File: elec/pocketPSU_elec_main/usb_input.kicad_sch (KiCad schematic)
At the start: 15 parts, among them J2 Conn_01x03_Pin, U4 FUSB302MPX

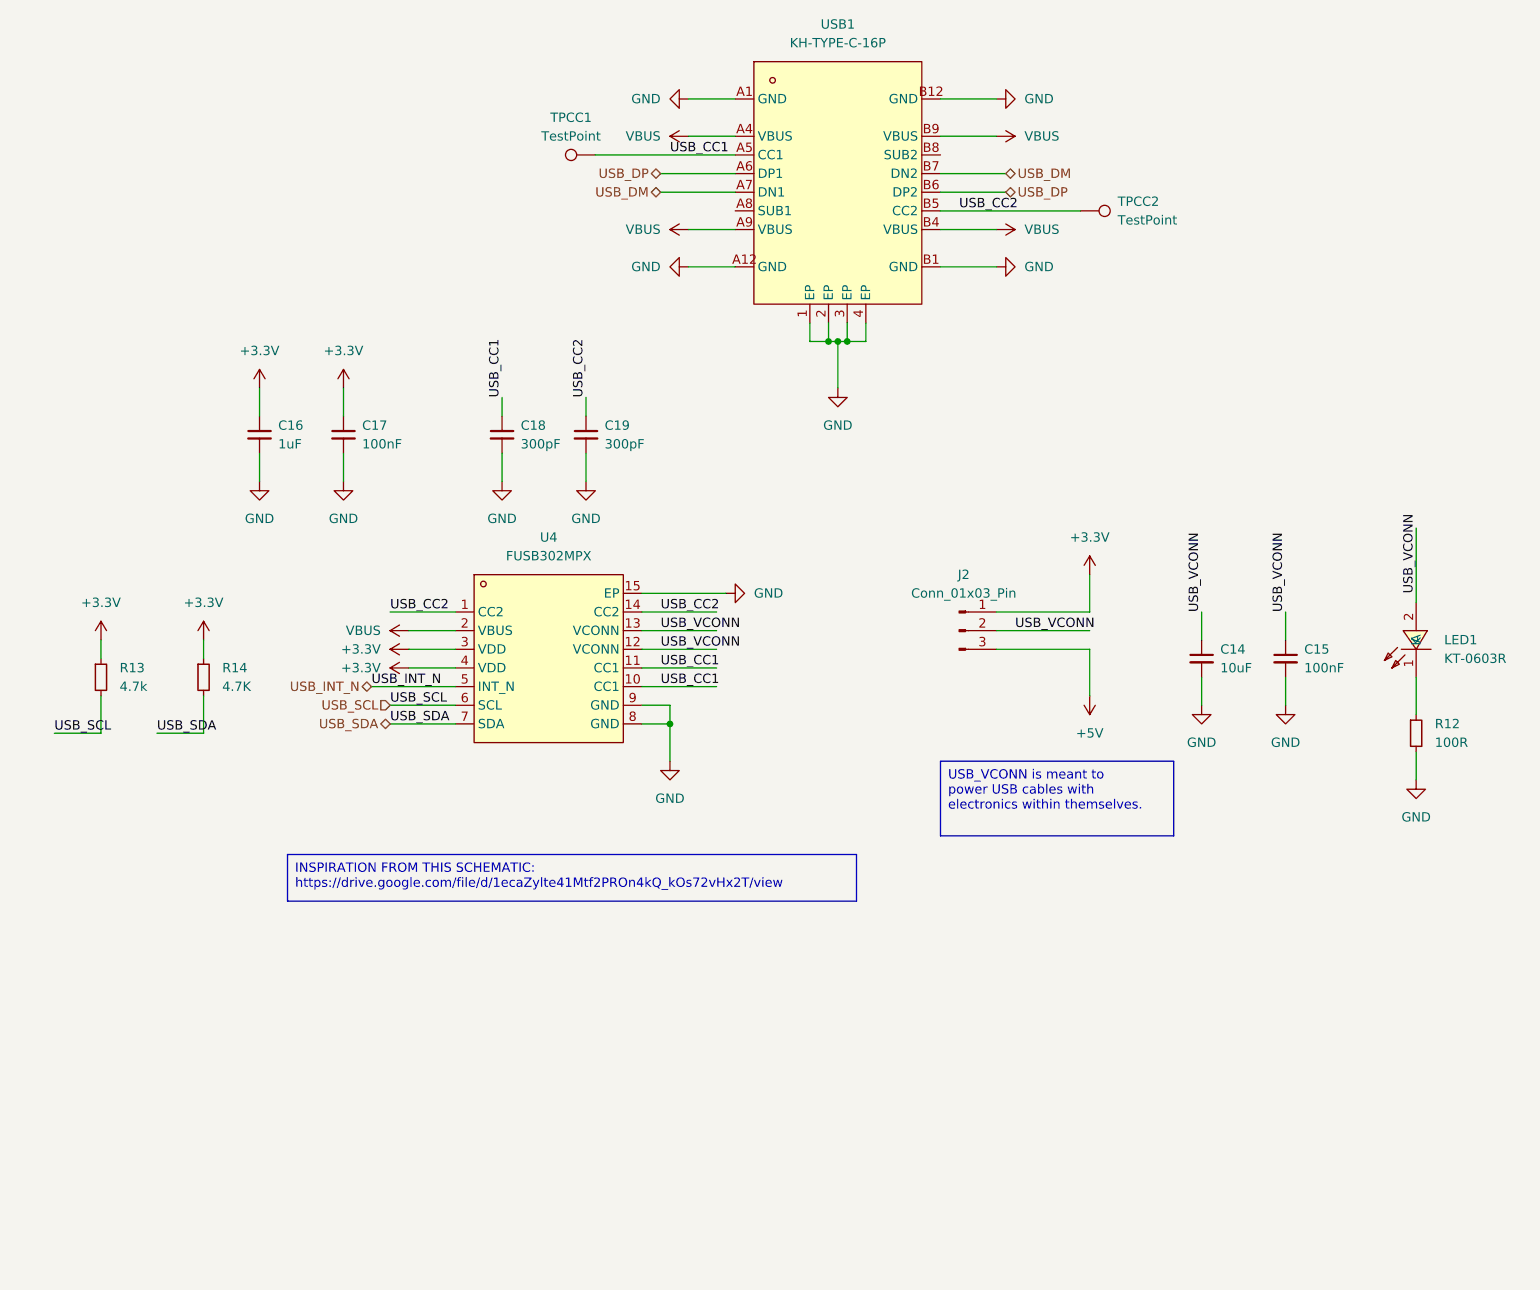
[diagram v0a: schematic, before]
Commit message: Cleanup, Buck, CAN (#6)
* mid-layout

* finished routing

* Kibot (#7)

Add kibot with JLC output generation

* fix 3d, add drc

* fix erc

* fix pcb drc

* drc ignore_unconnected

* attempt to add githash and tag

* add silk githash string

* add silk tag string

* change outputs

---------

Co-authored-by: Jarrod Tuma <jtuma@Jarrods-Laptop.local>
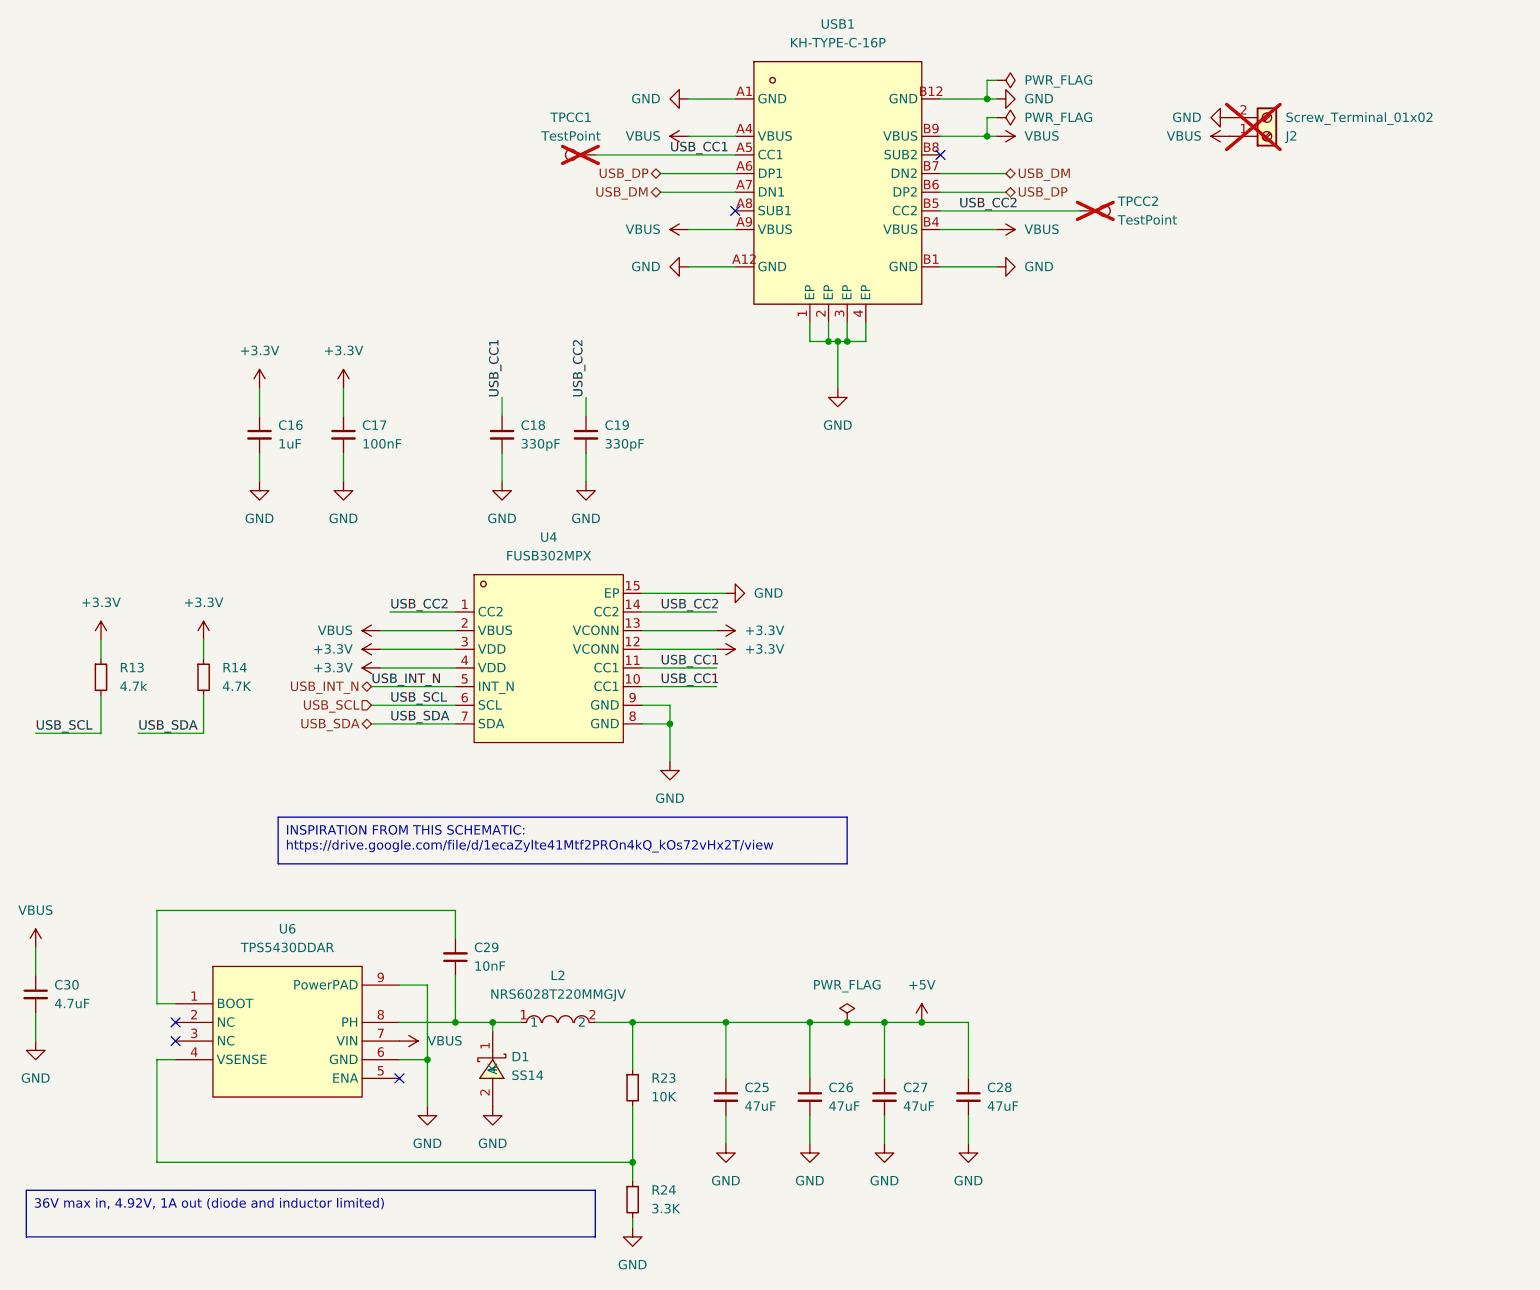
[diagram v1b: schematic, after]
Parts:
- removed C14: 10uF, Capacitor_SMD:C_0805_2012Metric, symbol Device:C_Small
- removed C15: 100nF, Capacitor_SMD:C_0805_2012Metric, symbol Device:C_Small
- removed J2: Conn_01x03_Pin, Connector_PinHeader_1.27mm:PinHeader_1x03_P1.27mm_Vertical, symbol Connector:Conn_01x03_Pin
- removed LED1: KT-0603R, footprints:LED0603-RD, symbol footprints:KT-0603R
- removed R12: 100R, Resistor_SMD:R_0402_1005Metric, symbol Device:R_Small
- added C25, C26, C27, C28: 47uF, Capacitor_SMD:C_1206_3216Metric, symbol Device:C_Small
- added C29: 10nF, Capacitor_SMD:C_0402_1005Metric, symbol Device:C_Small
- added C30: 4.7uF, Capacitor_SMD:C_1206_3216Metric, symbol Device:C_Small
- added D1: SS14, footprints:SMA_L4.2-W2.6-LS5.3-RD, symbol footprints:SS14
- added J2: Screw_Terminal_01x02, TerminalBlock_Phoenix:TerminalBlock_Phoenix_MPT-0,5-2-2.54_1x02_P2.54mm_Horizontal, symbol Connector:Screw_Terminal_01x02
- added L2: NRS6028T220MMGJV, footprints:IND-SMD_L6.0-W6.0, symbol footprints:NRS6028T220MMGJV
- added R23: 10K, Resistor_SMD:R_0402_1005Metric, symbol Device:R_Small
- added R24: 3.3K, Resistor_SMD:R_0402_1005Metric, symbol Device:R_Small
- added U6: TPS5430DDAR, footprints:ESOP-8_L4.9-W3.9-P1.27-LS6.0-TL-EP, symbol footprints:TPS5430DDAR
- C16: LCSC Part (none) -> C28323
- C17: LCSC Part (none) -> C49678
- C18, C19: value 300pF -> 330pF; footprint Capacitor_SMD:C_0805_2012Metric -> Capacitor_SMD:C_0603_1608Metric; LCSC Part (none) -> C1664
- R13, R14: LCSC Part (none) -> C25900
- TPCC1, TPCC2: now not fitted
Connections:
- net USB_VCONN is gone; now on net +3.3V: U4.12 (VCONN), U4.13 (VCONN)
- net +5V: now also C25.1, C26.1, C27.1, C28.1, L2.2, R23.1
- net GND: now also C25.2, C26.2, C27.2, C28.2, C30.2, D1.2 (A), J2.2 (Pin_2), R24.2, U6.6 (GND), U6.9 (PowerPAD)
- net VBUS: now also C30.1, J2.1 (Pin_1), U6.7 (VIN)
- new net: C29.1, D1.1 (K), L2.1, U6.8 (PH)
- new net: R23.2, R24.1, U6.4 (VSENSE)
- new net: C29.2, U6.1 (BOOT)
- no-connect marks 0 -> 5
